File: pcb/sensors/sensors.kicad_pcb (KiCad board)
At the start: 2 copper layers, 23.5 x 60 mm, 33 parts, among them J1 5V POWER, J10 PRESSURE, J3 CAN BUS, J4 DIMMER I2C, J5 DIMMER I2C, J6 FLOW HALL, J7 VALVE SSR, J8 BOILER SSR, Q2 AO3401A, Q3 2N7002, U1 XIAO ESP32-S3 / SOCKETED, U4 TJA1051T/3, U5 TMP102AIDRLR, U6 ADS1115IDGSR

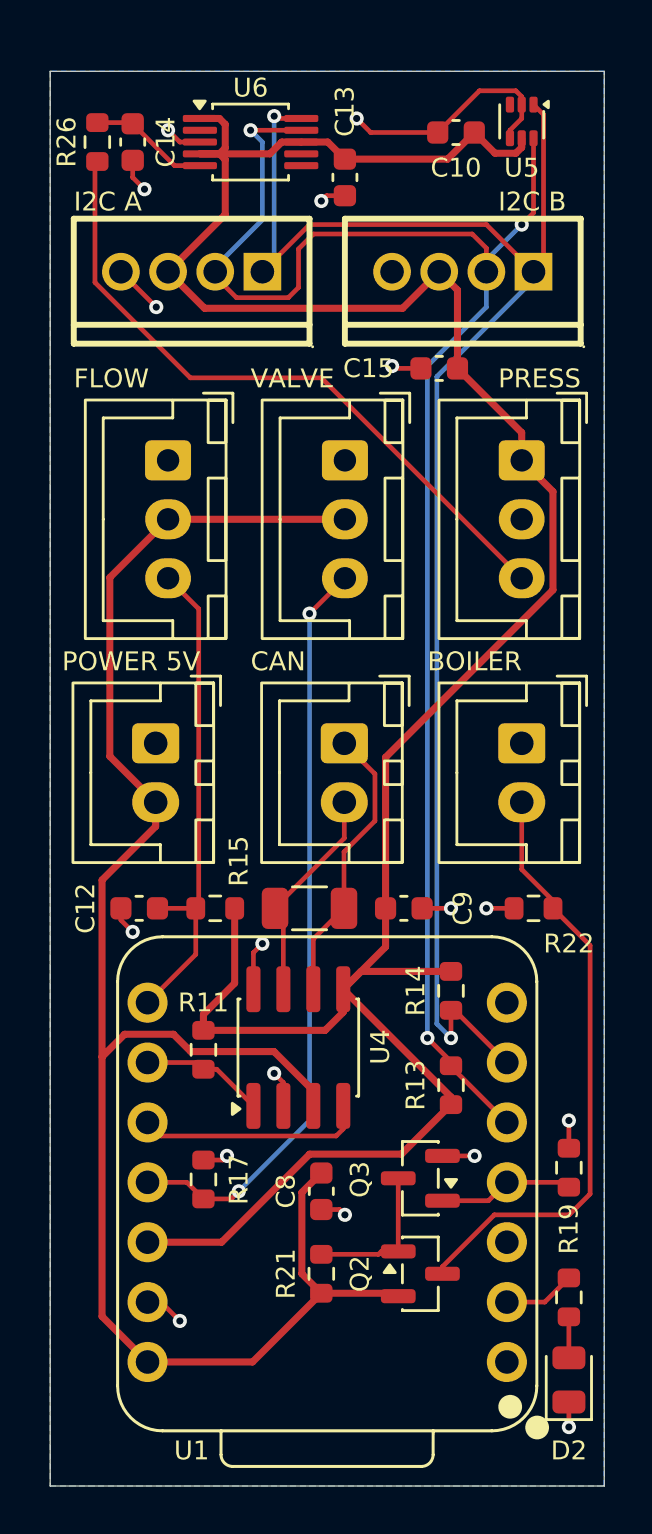
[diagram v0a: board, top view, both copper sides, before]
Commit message: Have JLCPCB solder the XIAO sockets and refresh sensors manufacturing
U1, the XIAO, stays in the schematic for its pinout but leaves the board.
Two female 1x7 sockets, J11 (XIAO pins 1-7) and J12 (pins 8-14), take its
fourteen holes with the same nets, so the routing is unchanged. They use
HX PM2.54-1x7P ZC-Y (C22438157) on a local footprint that keeps the tight
courtyard of the old U1 footprint; the XIAO outline becomes board silkscreen.

Bring sourcing and the BOM up to the XIAO board: drop the twenty
ESP32-S3-MINI parts, source C13-C15, J10, R26, U6 and the sockets, move D2
to the 0805 KT-0805G, refresh the catalog snapshot, and skip off-board
symbols in generate_bom.py. Rewrite customize-manufacturing.py for the J1-J12
references, without aliases or parity exceptions. The JLCPCB preview
confirmed every placement, with U6 and the sockets at +270 degrees and D2
without correction. Remove the files of the old export chain.

Co-Authored-By: Claude Opus 5.5 <noreply@anthropic.com>
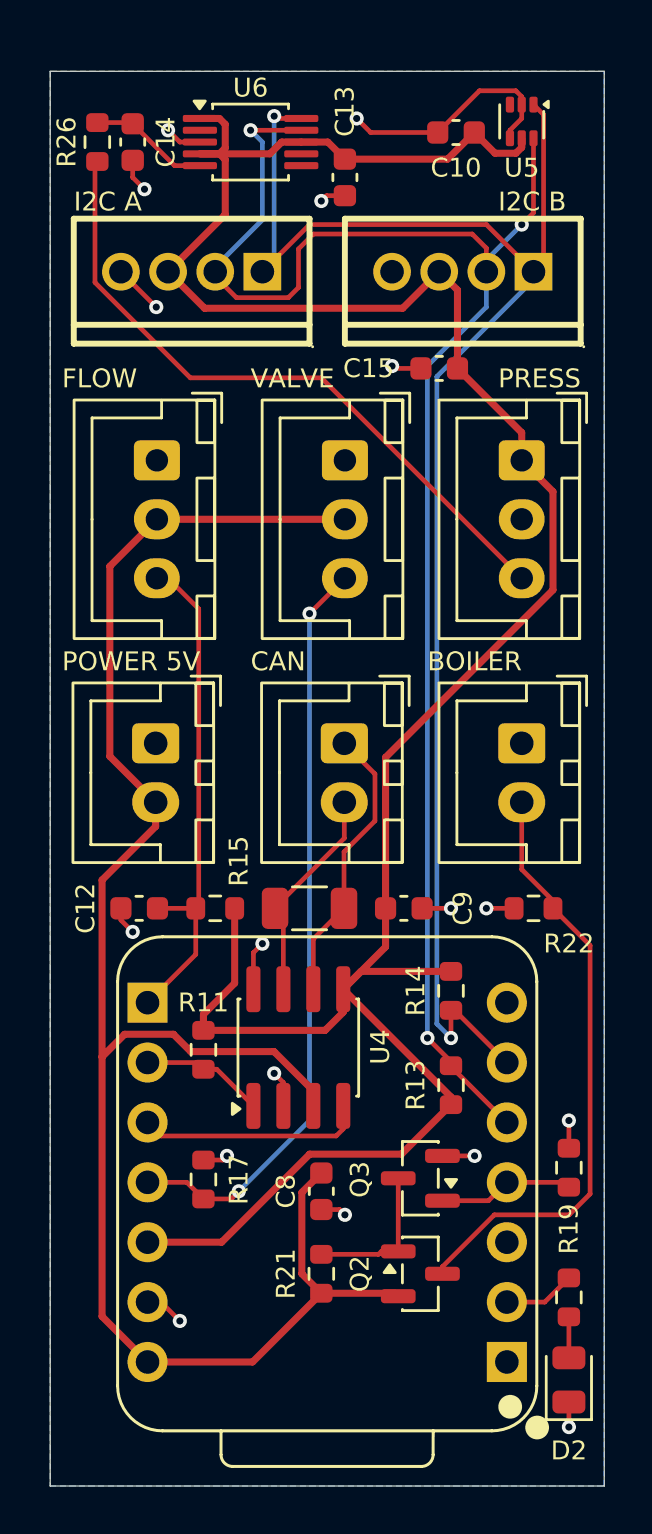
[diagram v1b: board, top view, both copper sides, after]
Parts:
- removed U1: XIAO ESP32-S3 / SOCKETED, Sensors_Local:XIAO-ESP32-S3-DIP-Headers
- added J11: XIAO D0-D6, Sensors_Local:XIAO_Socket_1x07_P2.54mm_Vertical, F.Cu at (228.9, 144.7)
- added J12: XIAO D7-5V, Sensors_Local:XIAO_Socket_1x07_P2.54mm_Vertical, F.Cu at (213.6, 129.5)
- moved J6 0.47 mm to (214.0, 106.5)

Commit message: Add an M2.5 mounting hole to the sensors board
H1 is a 2.7mm NPTH mounting hole for an M2.5 screw into a brass insert in
the printed enclosure, so the GND pour under the screw head needs no
keepout. The symbol stays out of the BOM, and generate_bom.py now skips
symbols excluded from the BOM so the hole does not break the UUID check.

Co-Authored-By: Claude Opus 5.5 <noreply@anthropic.com>
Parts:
- added H1: M2.5, MountingHole:MountingHole_2.7mm_M2.5, F.Cu at (222.0, 147.1)
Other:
- board size 23.5 x 60 mm -> 23.5 x 61 mm
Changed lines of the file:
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@@
 		)
 	)
+	(footprint "MountingHole:MountingHole_2.7mm_M2.5"
+		(layer "F.Cu")
+		(at 222 147.103038)
+		(descr "Mounting Hole 2.7mm, M2.5, no annular, generated by kicad-footprint-generator mountinghole.py")
+		(tags "mountinghole M2.5")
+		(property "Reference" "H1"
+			(at 4 -0.103038 0)
+			(layer "F.SilkS")
+			(hide yes)
+			(effects
+				(font
+					(size 1 1)
+					(thickness 0.15)
+				)
+			)
+		)
+		(property "Value" "M2.5"
+			(at 0 3.65 0)
+			(layer "F.Fab")
+			(effects
+				(font
+					(size 1 1)
+					(thickness 0.15)
+				)
+			)
+		)
+		(property "Datasheet" ""
+			(at 0 0 0)
+			(layer "F.Fab")
+			(hide yes)
+			(effects
+				(font
+					(size 1 1)
+					(thickness 0.15)
+				)
+			)
+		)
+		(property "Description" "Mounting Hole without connection"
+			(at 0 0 0)
+			(layer "F.Fab")
+			(hide yes)
+			(effects
+				(font
+					(size 1 1)
+					(thickness 0.15)
+				)
+			)
+		)
+		(property "KiLib_Generator" "mounting_hardware/mounting_hole"
+			(at 0 0 0)
+			(layer "F.SilkS")
+			(hide yes)
+			(effects
+				(font
+					(size 1 1)
+					(thickness 0.15)
+				)
+			)
+		)
+		(property "MPN" "M2.5 / 2.7mm"
+			(at 0 0 0)
+			(layer "F.Fab")
+			(hide yes)
+			(effects
+				(font
+					(size 1 1)
+					(thickness 0.15)
+				)
+			)
+		)
+		(sheetname "/")
+		(sheetfile "sensors.kicad_sch")
+		(attr exclude_from_pos_files exclude_from_bom)
+		(duplicate_pad_numbers_are_jumpers no)
+		(fp_circle
+			(center 0 0)
+			(end 2.7 0)
+			(stroke
+				(width 0.15)
+				(type solid)
+			)
+			(fill no)
+			(layer "Cmts.User")
+		)
+		(fp_circle
+			(center 0 0)
+			(end 2.95 0)
+			(stroke
+				(width 0.05)
+				(type solid)
+			)
+			(fill no)
+			(layer "F.CrtYd")
+		)
+		(fp_text user "${REFERENCE}"
+			(at 0 0 0)
+			(layer "F.Fab")
+			(effects
+				(font
+					(size 1 1)
+					(thickness 0.15)
+				)
+			)
+		)
+		(pad "" np_thru_hole circle
+			(at 0 0)
+			(size 2.7 2.7)
+			(drill 2.7)
+			(layers "*.Cu" "*.Mask")
+		)
+		(embedded_fonts no)
+	)
 	(footprint "Capacitor_SMD:C_0603_1608Metric"
 		(layer "F.Cu")
@@
 	)
 	(gr_line
-		(start 214.265 147.661)
-		(end 228.235 147.661)
-		(stroke
-			(width 0.1)
-			(type default)
-		)
-		(layer "F.SilkS")
-	)
-	(gr_line
-		(start 214.265 147.661)
-		(end 228.235 147.661)
-		(stroke
-			(width 0.127)
-			(type default)
-		)
-		(layer "F.SilkS")
-	)
-	(gr_line
-		(start 216.746 148.671)
-		(end 216.746 147.661)
-		(stroke
-			(width 0.127)
-			(type default)
-		)
-		(layer "F.SilkS")
-	)
-	(gr_arc
-		(start 217.246 149.171)
-		(mid 216.892447 149.024553)
-		(end 216.746 148.671)
-		(stroke
-			(width 0.127)
-			(type default)
-		)
-		(layer "F.SilkS")
-	)
-	(gr_line
-		(start 225.241272 149.171)
-		(end 217.246 149.171)
-		(stroke
-			(width 0.127)
-			(type default)
-		)
-		(layer "F.SilkS")
-	)
-	(gr_arc
-		(start 225.741272 148.671272)
-		(mid 225.594724 149.024644)
-		(end 225.241272 149.171)
-		(stroke
-			(width 0.127)
-			(type default)
-		)
-		(layer "F.SilkS")
-	)
-	(gr_line
-		(start 225.745 147.661)
-		(end 225.741272 148.671272)
-		(stroke
-			(width 0.127)
-			(type default)
-		)
-		(layer "F.SilkS")
-	)
-	(gr_line
 		(start 228.235 126.706)
 		(end 214.265 126.706)
@@
 	)
 	(gr_rect
-		(start 209.5 90)
+		(start 209.5 89)
 		(end 233 150)
 		(stroke
@@
 		(polygon
 			(pts
-				(xy 223 90) (xy 223 95) (xy 233 95) (xy 233 90)
+				(xy 223 89) (xy 223 95) (xy 233 95) (xy 233 89)
 			)
 		)
@@
 		(polygon
 			(pts
-				(xy 233 150) (xy 233 90) (xy 209.5 90) (xy 209.5 150)
+				(xy 233 150) (xy 233 89) (xy 209.5 89) (xy 209.5 150)
 			)
 		)
